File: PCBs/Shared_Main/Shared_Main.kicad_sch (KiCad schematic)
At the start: 18 parts, among them J1 Power, J16 Other unit, J4 Aux, J5 Analog inputs, J7 Keypad, U1 ESP32-S3-ZERO, U2 74HC4051

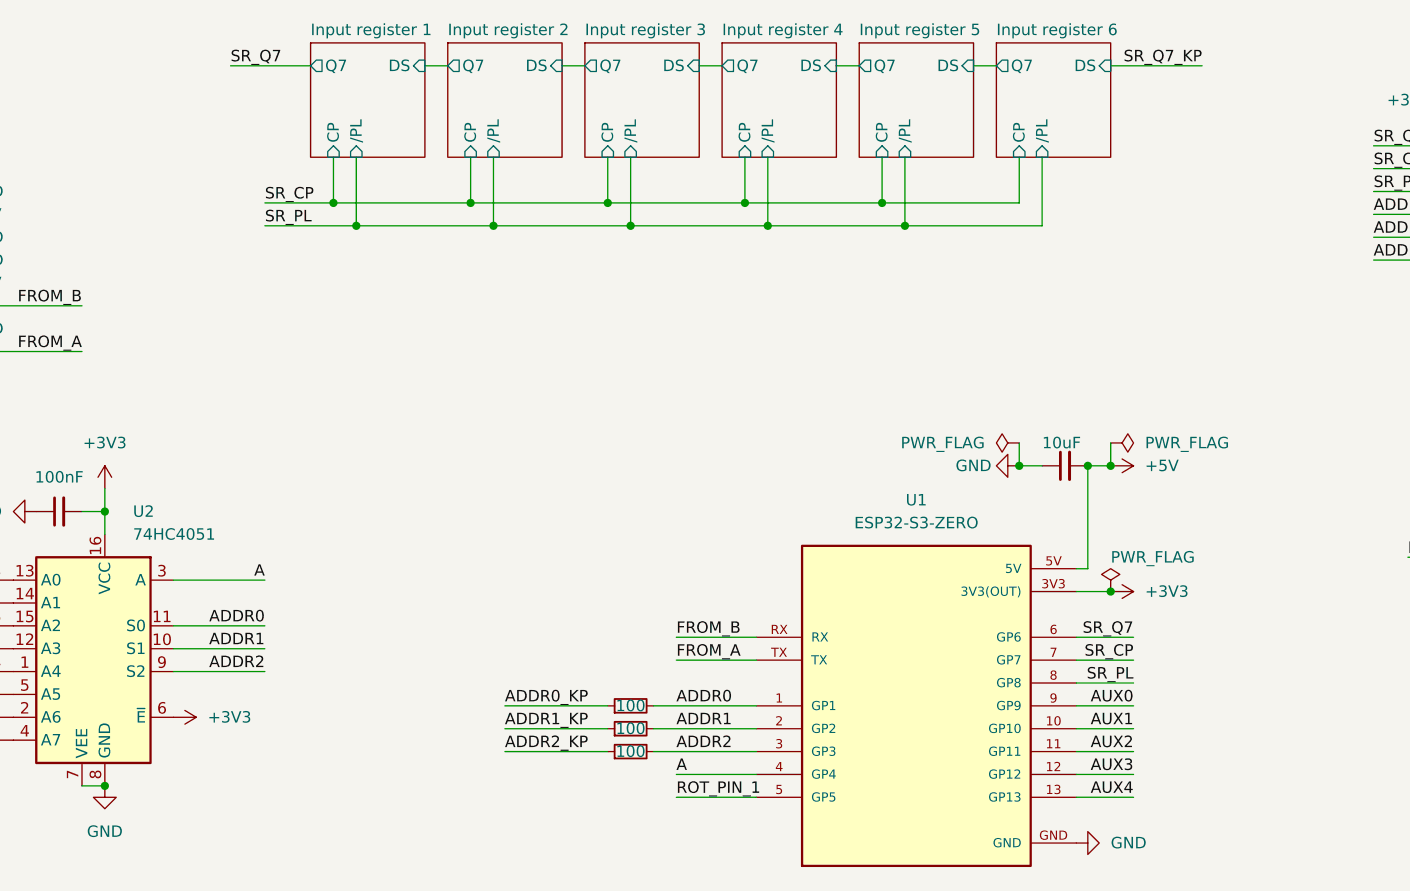
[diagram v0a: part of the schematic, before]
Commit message: Fix 74HC4051 enable, set pull-up values, name keypad column nets
Shared_Main:
- U2 (74HC4051) pin 6 (~E) was tied to +3V3, permanently inhibiting all
  eight analog channels. Moved to GND. The pad had no tracks on it, so
  the board change is just which plane claims it (In2 +3V3 -> In1 GND);
  all zones refilled.
- RN1-RN6 pull-up arrays had no value assigned (still reading the
  R_Network08 symbol default). Set to 10k, matching RN8. Board footprint
  value fields synced to match.
- Also includes graphical tidy-up of junction/wire placement (no netlist
  change).

Right_Keypad:
- RN1 pull-up array set to 10k, board field synced.
- U1 was using a locally modified 74HC165 whose D0-D3 pins had been moved
  (via Swap Pins) so the column rails fan out to RN1 without crossing.
  That recorded the bit-order decision in pin geometry, where nothing
  diffs it and an "Update Symbols from Library" would silently remap four
  nets. Reverted U1 to the stock 74xx:74HC165 and expressed the same
  mapping as named nets COL1-COL8 instead:

      COL1 -> D3   COL5 -> D4
      COL2 -> D2   COL6 -> D5
      COL3 -> D1   COL7 -> D6
      COL4 -> D0   COL8 -> D7

  Connectivity is unchanged - verified by diffing before/after netlists
  with net names stripped and each net's pin set sorted. No copper moved
  (363 segments, 8 vias, 57 footprints before and after); only net names
  changed on the board.

Both projects: ERC 0, DRC 0, 0 unconnected, 0 schematic parity issues.

Co-Authored-By: Claude Opus 5 <noreply@anthropic.com>
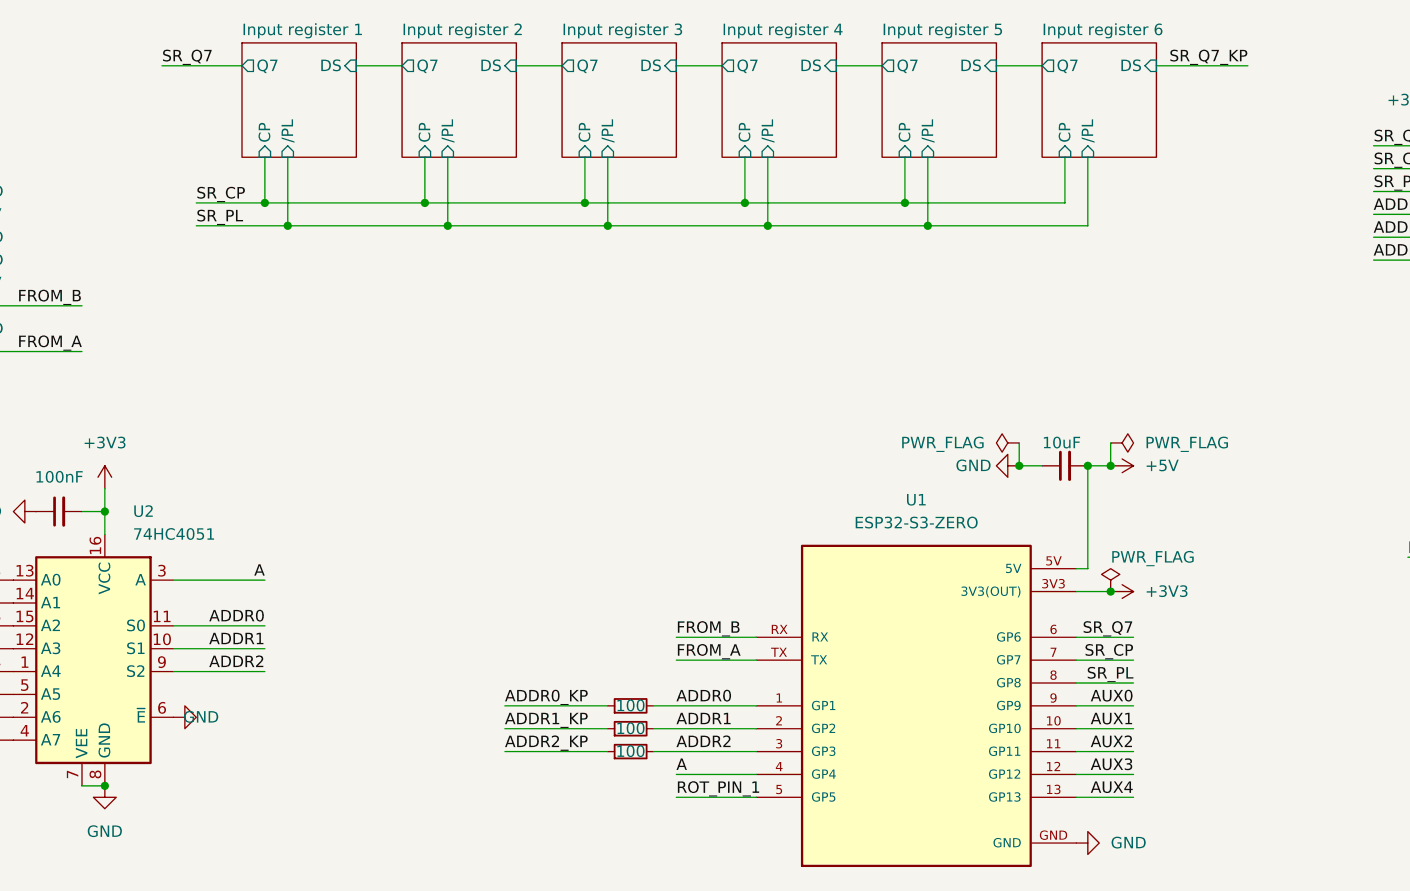
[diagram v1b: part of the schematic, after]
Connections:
- net +3V3: no longer U2.6 (~{E})
- net GND: now also U2.6 (~{E})
